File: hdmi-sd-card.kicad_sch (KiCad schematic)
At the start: 94 parts, among them J11 I-PEX_CABLINE-VS_1x20_20455-A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, J4 HDMI-A_WE_685119134923, J5 MicroSD_693071020811, Q18 BSS138PW, Q19 BSS138PW, Q21 BSS138PW, U10 TPD4E05U06QDQARQ1, U11 TPD4E05U06QDQARQ1, U37 TPD4E05U06QDQARQ1, U38 SN65DP159RGZR, U40 NVT4858_XQFN, U41 TPD4E05U06QDQARQ1, U42 M24C64-F_DFN8, U43 TPS2116DRLR, U44 TXS0102DQER, U47 TPD4E05U06QDQARQ1, U48 TPD4E05U06QDQARQ1

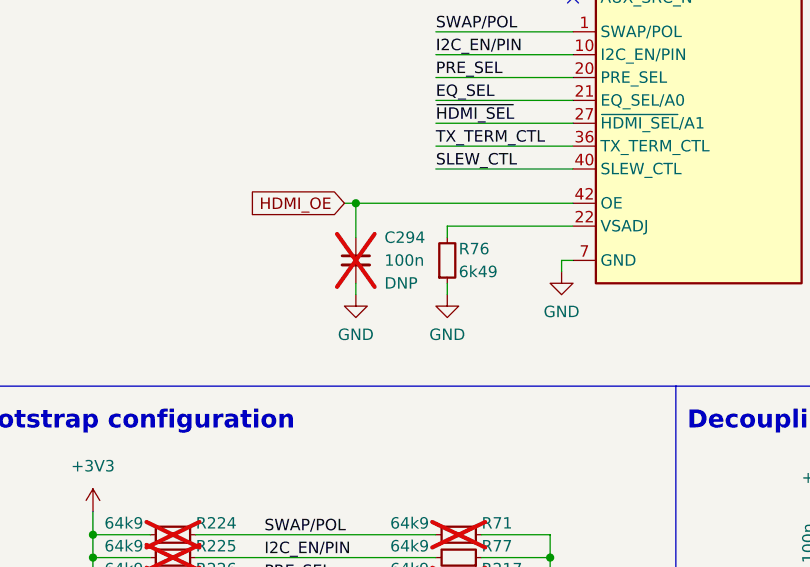
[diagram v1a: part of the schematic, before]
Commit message: [#69629] Fix DNP attributes
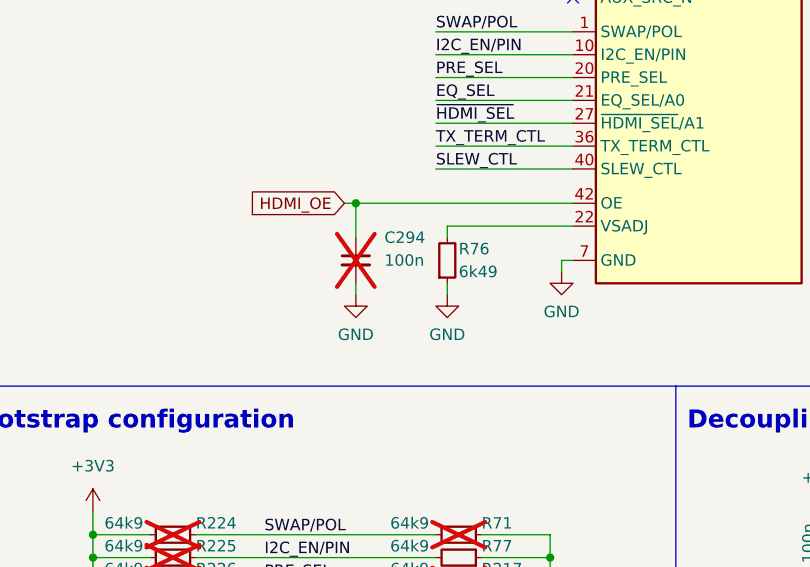
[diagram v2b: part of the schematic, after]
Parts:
- C294: DNP DNP -> (none); now left out of the parts list
- R217, R221, R225, R226, R230: now left out of the parts list

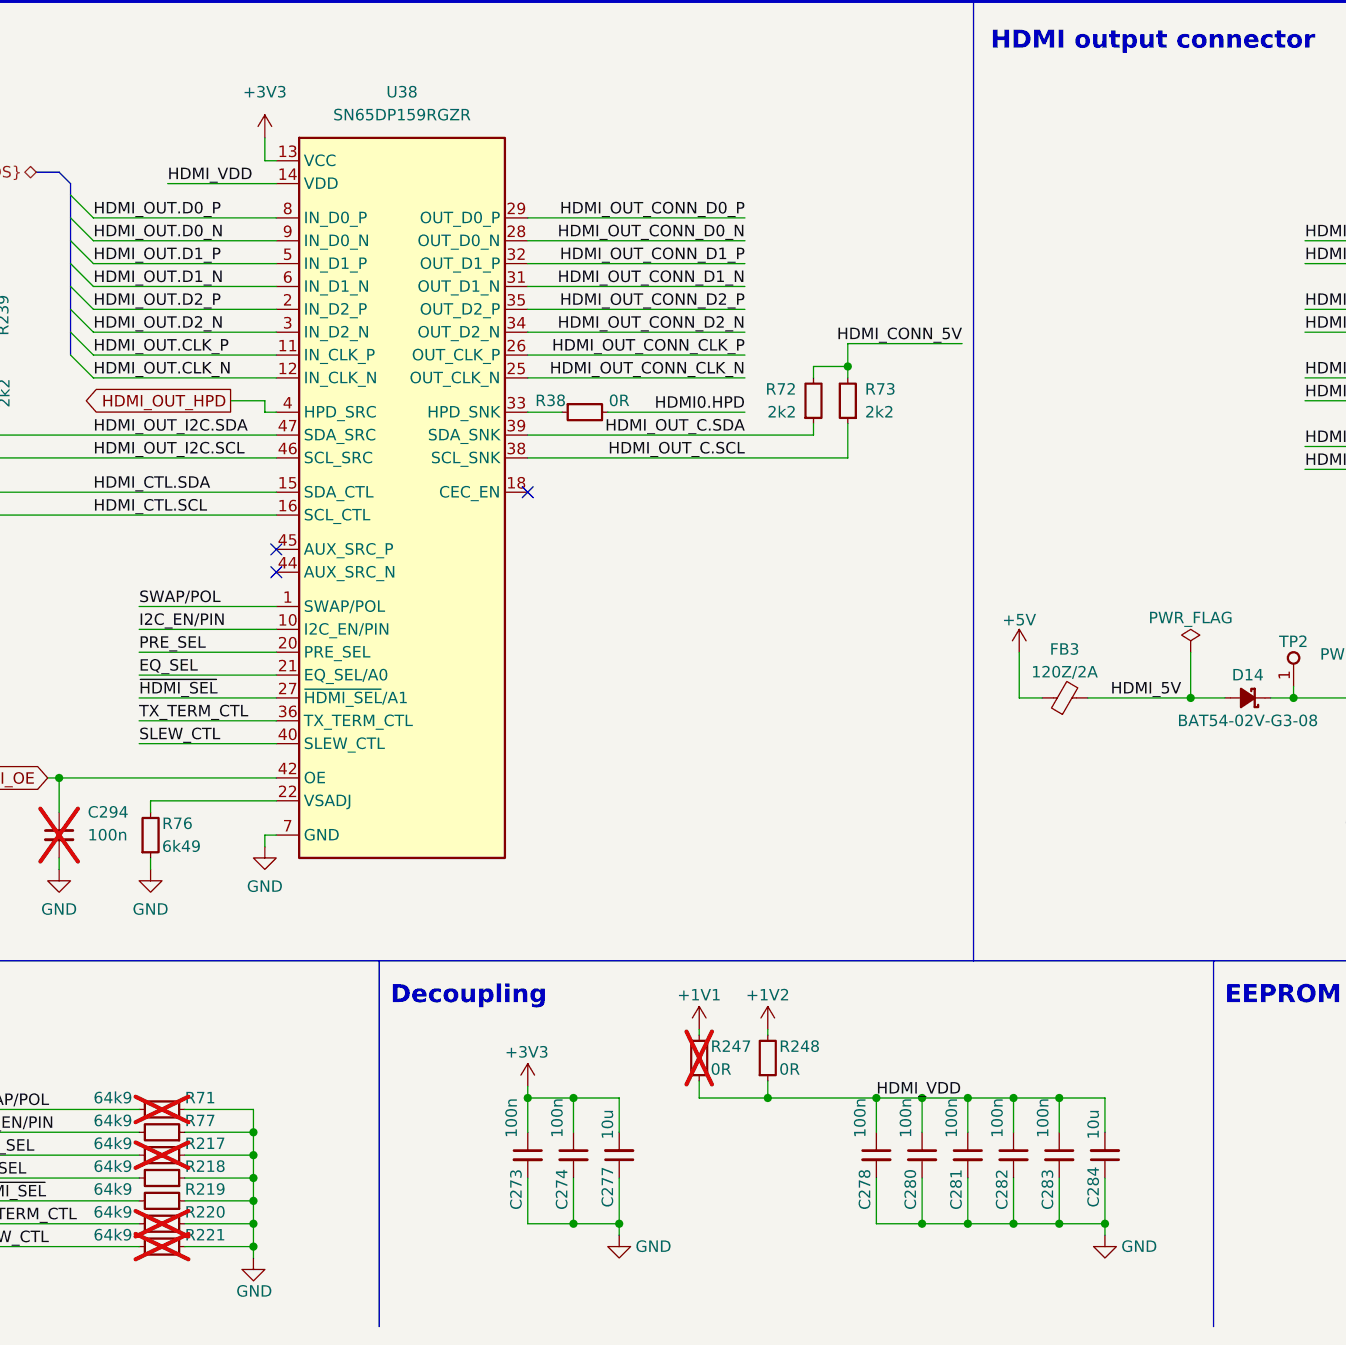
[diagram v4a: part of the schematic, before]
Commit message: [#70506] Clean DRC and ERC
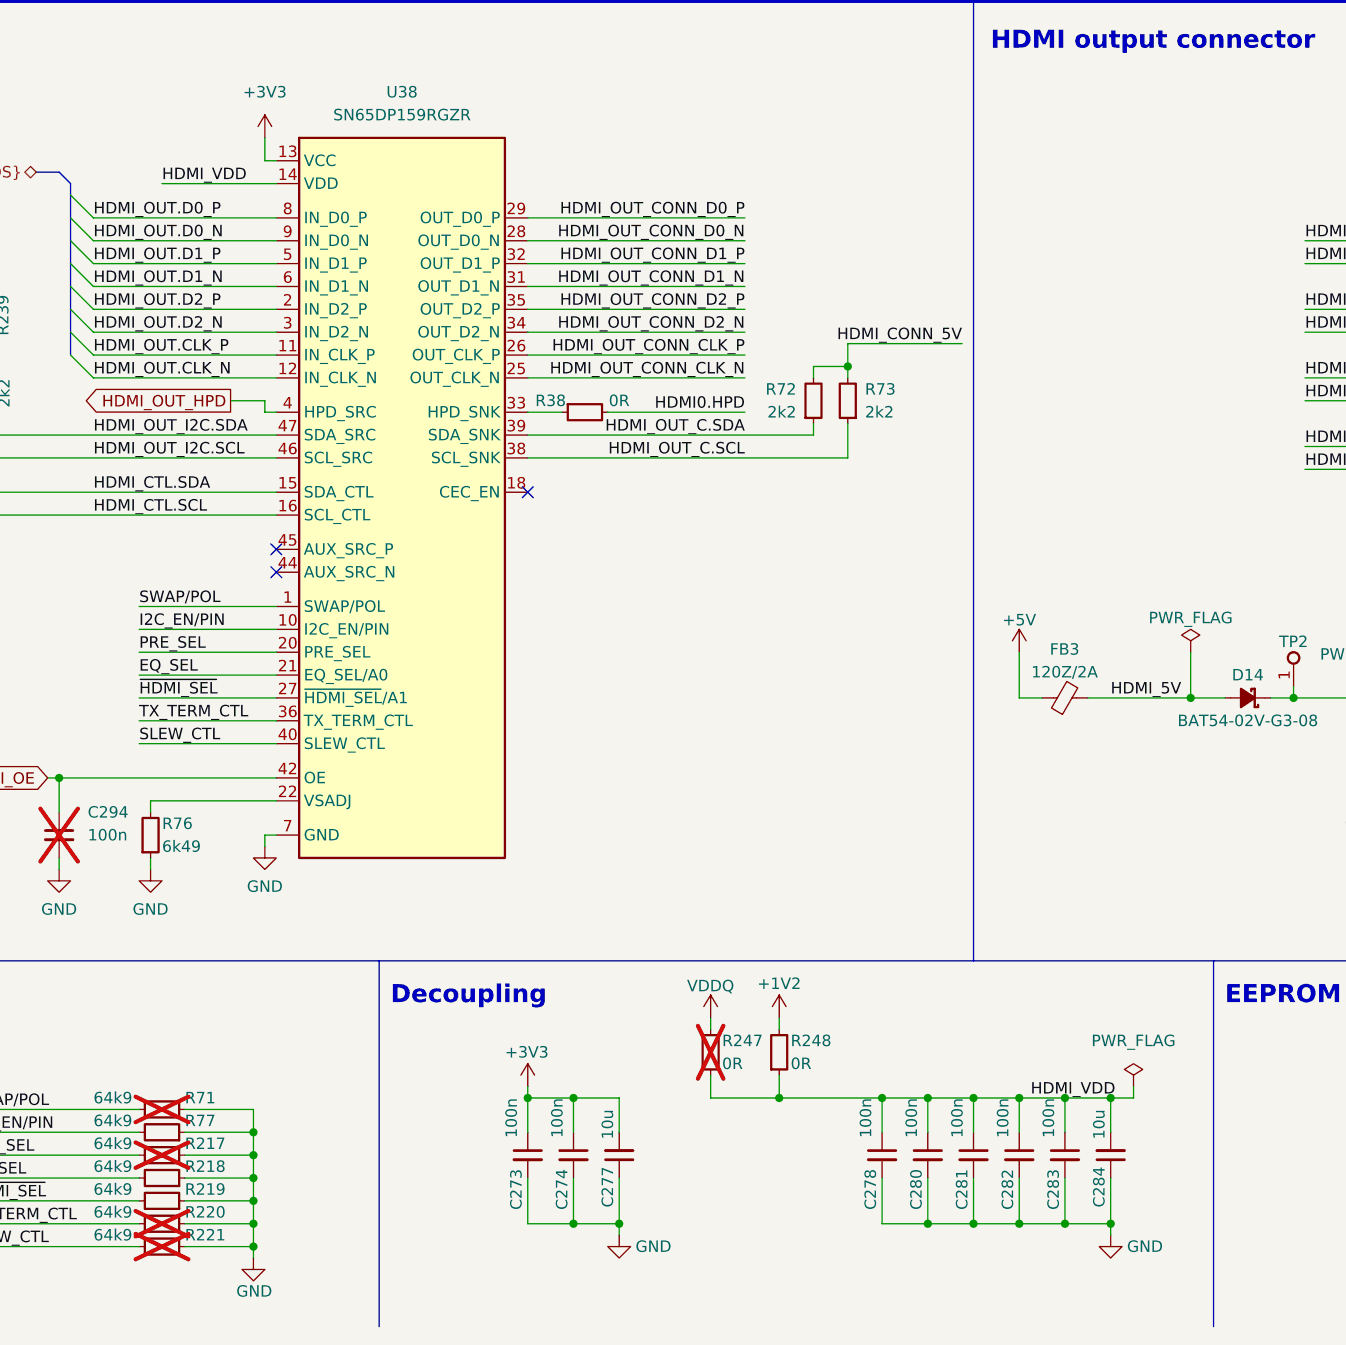
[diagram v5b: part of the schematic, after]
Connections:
- net +1V1 renamed VDDQ
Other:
- moved on the sheet: C278, C280, C281, C282, C283, C284, R247, R248
